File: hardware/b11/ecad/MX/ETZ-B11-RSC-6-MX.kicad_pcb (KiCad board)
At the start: 2 copper layers, 112.3 x 85.8 mm, 36 parts, among them SW1 MX-Hotswap-1U, SW10 MX-Hotswap-1U, SW11 MX-Hotswap-1U, SW12 MX-Hotswap-1U, SW13 MX-Hotswap-1U, SW14 MX-Hotswap-1U, SW15 MX-Hotswap-1U, SW16 MX-Hotswap-1U, SW17 MX-Hotswap-1U, SW18 MX-Hotswap-1U, SW2 MX-Hotswap-1U, SW3 MX-Hotswap-1U, SW4 MX-Hotswap-1U, SW5 MX-Hotswap-1U, SW6 MX-Hotswap-1U, SW7 MX-Hotswap-1U, SW8 MX-Hotswap-1U, SW9 MX-Hotswap-1U

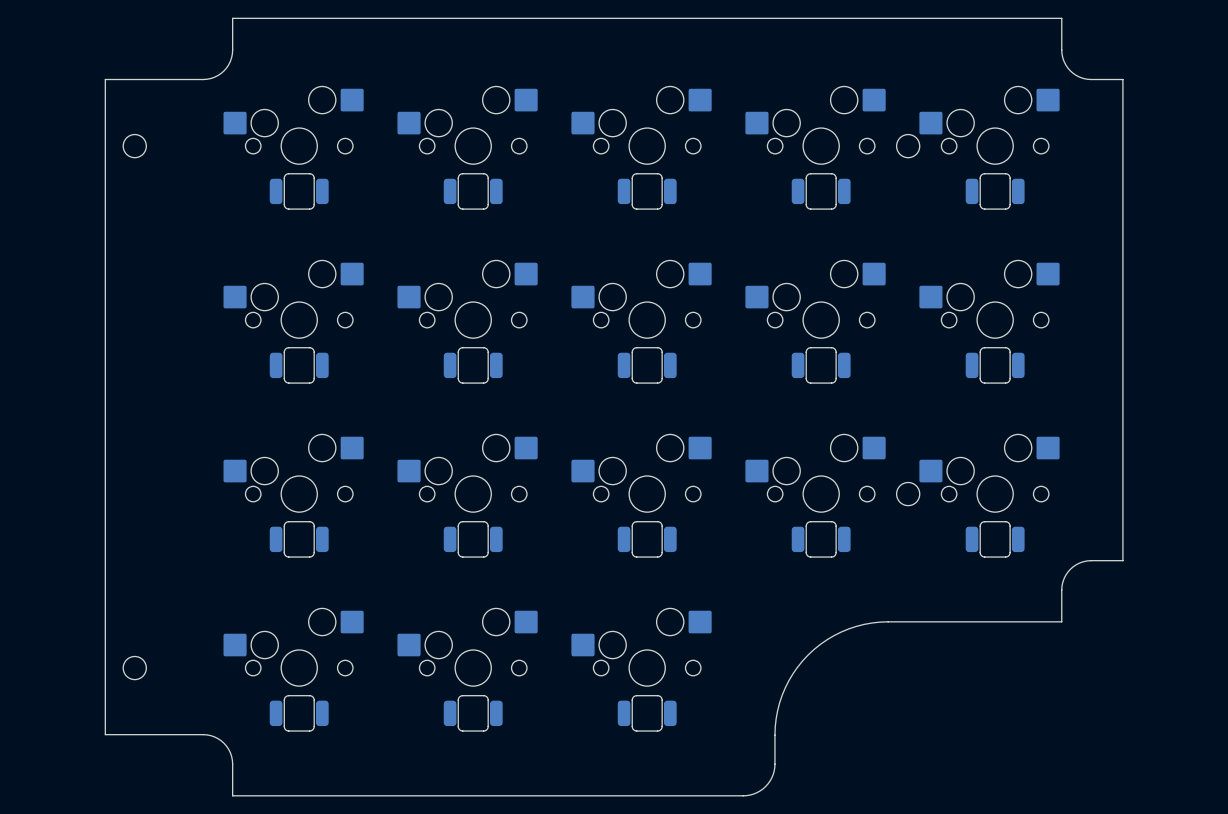
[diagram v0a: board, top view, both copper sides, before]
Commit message: refactor(hardware/b11): restructure ecad + tools, add KS-33 boards
- Rename PCB files: *-N → *-MX, *-L → *-CHOC-V2
- Reorganise ecad/ into per-family subfolders (MX/, CHOC-V2/, KS-33/)
- Add 8 blank KS-33 boards (outline only, human-populated ad-hoc)
- Apply JLCPCB-validated stackup (white/black/FR4 natural/black/white)
  to all 24 boards; SP boards at correct family thickness
- Add hardware/b11/tools/: config.py, placement.py, place-switch-sockets.py,
  place-switch-leds.py, place-display-leds.py — family-aware, non-destructive
- Archive old placement + generation scripts to hardware/scripts/_archive/
- Remove switch-origins.yaml (replaced by GRID_ORIGINS in config.py)
- Add PLAN.md tracking refactor progress

Co-Authored-By: Claude Sonnet 4.6 <noreply@anthropic.com>
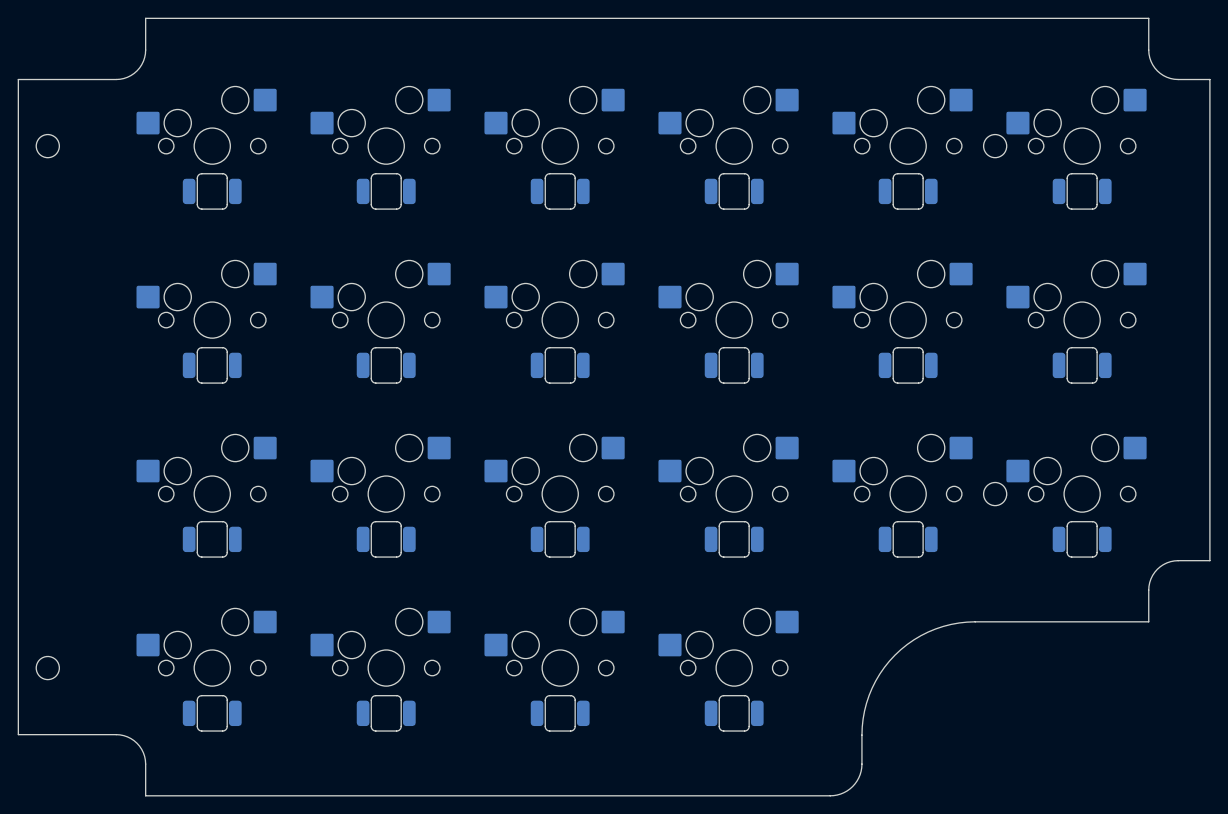
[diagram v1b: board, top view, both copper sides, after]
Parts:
- added LED19: LED_SMD_6028_BackMount, LED_SMD_6028_BackMount, B.Cu at (161.8, 135.9)
- added LED20: LED_SMD_6028_BackMount, LED_SMD_6028_BackMount, B.Cu at (142.6, 135.9)
- added LED21: LED_SMD_6028_BackMount, LED_SMD_6028_BackMount, B.Cu at (123.3, 135.9)
- added LED22: LED_SMD_6028_BackMount, LED_SMD_6028_BackMount, B.Cu at (104.2, 135.9)
- added SW19: MX-Hotswap-1U, MX-Hotswap-1U, F.Cu at (161.8, 130.9)
- added SW20: MX-Hotswap-1U, MX-Hotswap-1U, F.Cu at (142.6, 130.9)
- added SW21: MX-Hotswap-1U, MX-Hotswap-1U, F.Cu at (123.3, 130.9)
- added SW22: MX-Hotswap-1U, MX-Hotswap-1U, F.Cu at (104.2, 130.9)
- moved LED6 88.5 mm to (104.2, 78.3)
- moved SW6 88.5 mm to (104.2, 73.3)
- moved LED11 69.9 mm to (123.3, 97.5)
- moved SW11 69.9 mm to (123.3, 92.5)
- moved LED12 69.9 mm to (104.2, 97.5)
- moved SW12 69.9 mm to (104.2, 92.5)
- moved LED13 48.0 mm to (200.2, 116.7)
- moved LED14 48.0 mm to (180.9, 116.7)
- moved LED15 48.0 mm to (161.8, 116.7)
- moved SW13 48.0 mm to (200.2, 111.7)
- moved SW14 48.0 mm to (180.9, 111.7)
- moved SW15 48.0 mm to (161.8, 111.7)
- moved LED10 28.8 mm to (142.6, 97.5)
- moved LED7 28.8 mm to (200.2, 97.5)
- moved LED9 28.8 mm to (161.8, 97.5)
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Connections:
- SW10 pad 2: COL4 -> COL3
- SW11 pad 1: ROW2 -> ROW1
- SW11 pad 2: COL0 -> COL4
- SW12 pad 1: ROW2 -> ROW1
- SW12 pad 2: COL1 -> COL5
- SW13 pad 2: COL2 -> COL0
- SW14 pad 2: COL3 -> COL1
- SW15 pad 2: COL4 -> COL2
- SW16 pad 1: ROW3 -> ROW2
- SW16 pad 2: COL2 -> COL3
- SW17 pad 1: ROW3 -> ROW2
- SW17 pad 2: COL3 -> COL4
- SW18 pad 1: ROW3 -> ROW2
- SW18 pad 2: COL4 -> COL5
- SW6 pad 1: ROW1 -> ROW0
- SW6 pad 2: COL0 -> COL5
- SW7 pad 2: COL1 -> COL0
- SW8 pad 2: COL2 -> COL1
- SW9 pad 2: COL3 -> COL2
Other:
- board size 112.3 x 85.8 mm -> 131.5 x 85.8 mm
